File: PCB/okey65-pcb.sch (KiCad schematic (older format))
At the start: 152 parts, among them J1 USB_C_Receptacle_USB2.0, SW1 SW_Push, U1 ATmega32U4-AU, Y1 16MHz

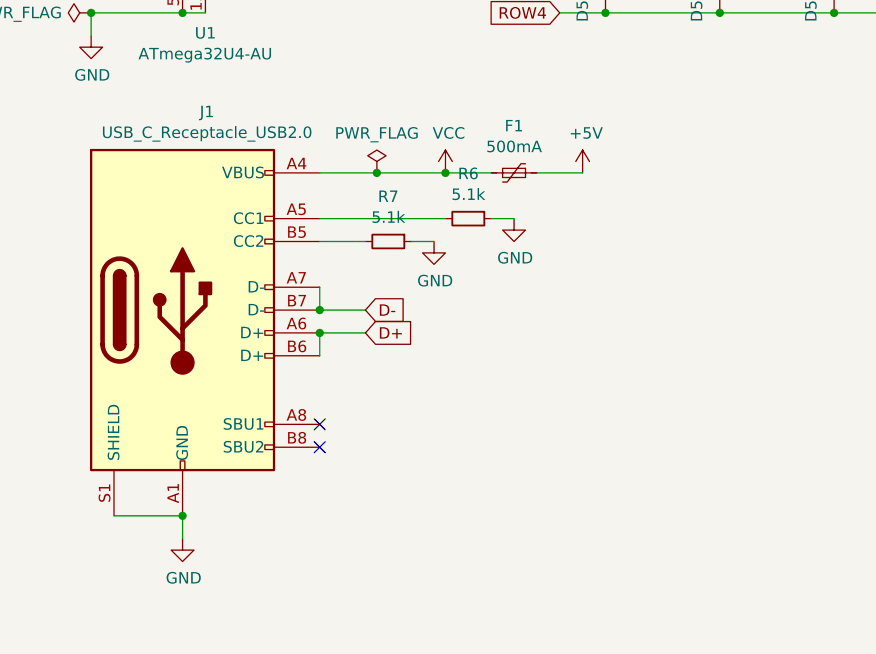
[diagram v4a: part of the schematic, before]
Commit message: General improvements - no ground planes
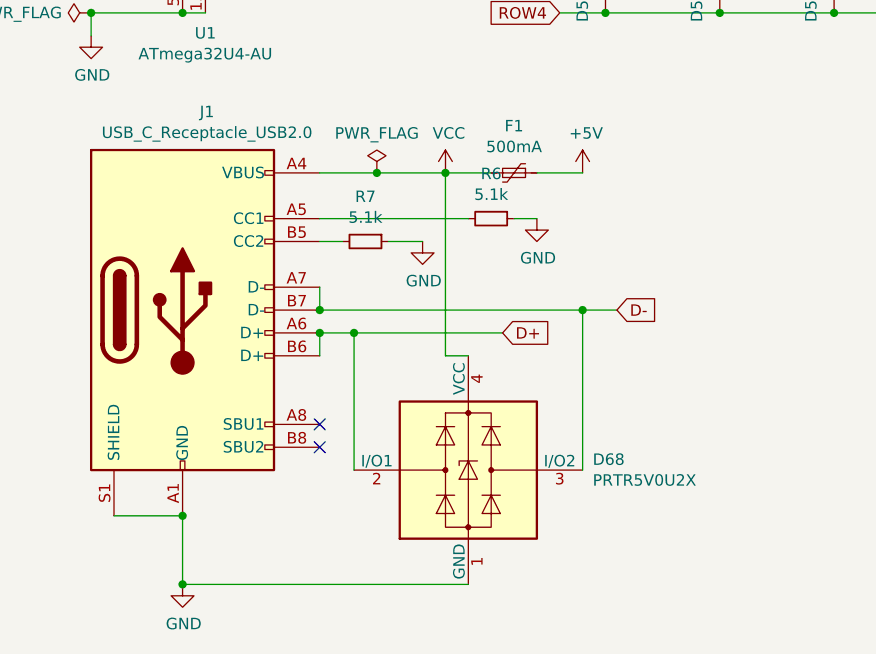
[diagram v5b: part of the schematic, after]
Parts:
- added D68: PRTR5V0U2X, random-keyboard-parts:SOT143B, symbol Power_Protection:PRTR5V0U2X
- C7: footprint Capacitor_SMD:C_0805_2012Metric -> Capacitor_SMD:C_1206_3216Metric
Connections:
- net D+: now also D68.2 (I/O1)
- net D-: now also D68.3 (I/O2)
- net GND: now also D68.1 (GND)
- net VCC: now also D68.4 (VCC)
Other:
- moved on the sheet: R6, R7
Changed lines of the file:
@@
 F 0 "C7" H 1992 4296 50  0000 L CNN
 F 1 "10uF" H 1992 4205 50  0000 L CNN
-F 2 "Capacitor_SMD:C_0805_2012Metric" H 1900 4250 50  0001 C CNN
+F 2 "Capacitor_SMD:C_1206_3216Metric" H 1900 4250 50  0001 C CNN
 F 3 "~" H 1900 4250 50  0001 C CNN
 F 4 "C77075" H 1900 4250 50  0001 C CNN "LCSC"
@@
 Wire Wire Line
 	4200 5700 4400 5700
-Text GLabel 3450 6400 2    50   Input ~ 0
+Text GLabel 4050 6400 2    50   Input ~ 0
 D+
-Text GLabel 3450 6300 2    50   Input ~ 0
+Text GLabel 4550 6300 2    50   Input ~ 0
 D-
 Wire Wire Line
 	3250 6200 3250 6300
 Wire Wire Line
-	3250 6300 3450 6300
+	3250 6300 4400 6300
 Connection ~ 3250 6300
 Wire Wire Line
 	3250 6500 3250 6400
 Wire Wire Line
-	3250 6400 3450 6400
+	3250 6400 3400 6400
 Connection ~ 3250 6400
 $Comp
 L power:GND #PWR017
 U 1 1 61C37D79
-P 2650 7300
-F 0 "#PWR017" H 2650 7050 50  0001 C CNN
-F 1 "GND" H 2655 7127 50  0000 C CNN
-F 2 "" H 2650 7300 50  0001 C CNN
-F 3 "" H 2650 7300 50  0001 C CNN
-	1    2650 7300
+P 2650 7500
+F 0 "#PWR017" H 2650 7250 50  0001 C CNN
+F 1 "GND" H 2655 7327 50  0000 C CNN
+F 2 "" H 2650 7500 50  0001 C CNN
+F 3 "" H 2650 7500 50  0001 C CNN
+	1    2650 7500
 	1    0    0    -1
 $EndComp
 Wire Wire Line
 	2350 7200 2650 7200
-Wire Wire Line
-	2650 7200 2650 7300
-Connection ~ 2650 7200
 $Comp
 L Device:R_Small R7
 U 1 1 61C3A76B
-P 3550 6000
-F 0 "R7" V 3354 6000 50  0000 C CNN
-F 1 "5.1k" V 3445 6000 50  0000 C CNN
-F 2 "Resistor_SMD:R_0805_2012Metric" H 3550 6000 50  0001 C CNN
-F 3 "~" H 3550 6000 50  0001 C CNN
-F 4 "C27834" H 3550 6000 50  0001 C CNN "LCSC"
-	1    3550 6000
+P 3450 6000
+F 0 "R7" V 3254 6000 50  0000 C CNN
+F 1 "5.1k" V 3345 6000 50  0000 C CNN
+F 2 "Resistor_SMD:R_0805_2012Metric" H 3450 6000 50  0001 C CNN
+F 3 "~" H 3450 6000 50  0001 C CNN
+F 4 "C27834" H 3450 6000 50  0001 C CNN "LCSC"
+	1    3450 6000
 	0    1    1    0
 $EndComp
@@
 L Device:R_Small R6
 U 1 1 61C3B0BC
-P 3900 5900
-F 0 "R6" V 3704 5900 50  0000 C CNN
-F 1 "5.1k" V 3795 5900 50  0000 C CNN
-F 2 "Resistor_SMD:R_0805_2012Metric" H 3900 5900 50  0001 C CNN
-F 3 "~" H 3900 5900 50  0001 C CNN
-F 4 "C27834" H 3900 5900 50  0001 C CNN "LCSC"
-	1    3900 5900
+P 4000 5900
+F 0 "R6" V 3804 5900 50  0000 C CNN
+F 1 "5.1k" V 3895 5900 50  0000 C CNN
+F 2 "Resistor_SMD:R_0805_2012Metric" H 4000 5900 50  0001 C CNN
+F 3 "~" H 4000 5900 50  0001 C CNN
+F 4 "C27834" H 4000 5900 50  0001 C CNN "LCSC"
+	1    4000 5900
 	0    1    1    0
 $EndComp
@@
 L power:GND #PWR014
 U 1 1 61C3D0EA
-P 4100 5900
-F 0 "#PWR014" H 4100 5650 50  0001 C CNN
-F 1 "GND" H 4105 5727 50  0000 C CNN
-F 2 "" H 4100 5900 50  0001 C CNN
-F 3 "" H 4100 5900 50  0001 C CNN
-	1    4100 5900
+P 4200 5900
+F 0 "#PWR014" H 4200 5650 50  0001 C CNN
+F 1 "GND" H 4205 5727 50  0000 C CNN
+F 2 "" H 4200 5900 50  0001 C CNN
+F 3 "" H 4200 5900 50  0001 C CNN
+	1    4200 5900
 	1    0    0    -1
 $EndComp
@@
 L power:GND #PWR015
 U 1 1 61C3DC0E
-P 3750 6000
-F 0 "#PWR015" H 3750 5750 50  0001 C CNN
-F 1 "GND" H 3755 5827 50  0000 C CNN
-F 2 "" H 3750 6000 50  0001 C CNN
-F 3 "" H 3750 6000 50  0001 C CNN
-	1    3750 6000
-	1    0    0    -1
-$EndComp
-Wire Wire Line
-	3250 5900 3800 5900
-Wire Wire Line
-	4000 5900 4100 5900
-Wire Wire Line
-	3250 6000 3450 6000
-Wire Wire Line
-	3650 6000 3750 6000
+P 3700 6000
+F 0 "#PWR015" H 3700 5750 50  0001 C CNN
+F 1 "GND" H 3705 5827 50  0000 C CNN
+F 2 "" H 3700 6000 50  0001 C CNN
+F 3 "" H 3700 6000 50  0001 C CNN
+	1    3700 6000
+	1    0    0    -1
+$EndComp
+Wire Wire Line
+	3250 5900 3900 5900
+Wire Wire Line
+	3250 6000 3350 6000
+Wire Wire Line
+	3550 6000 3700 6000
 NoConn ~ 3250 6800
 NoConn ~ 3250 6900
@@
 Connection ~ 2650 1250
 Connection ~ 2650 1400
+$Comp
+L Power_Protection:PRTR5V0U2X D68
+U 1 1 61C886DE
+P 3900 7000
+F 0 "D68" H 4444 7046 50  0000 L CNN
+F 1 "PRTR5V0U2X" H 4444 6955 50  0000 L CNN
+F 2 "random-keyboard-parts:SOT143B" H 3960 7000 50  0001 C CNN
+F 3 "https://assets.nexperia.com/documents/data-sheet/PRTR5V0U2X.pdf" H 3960 7000 50  0001 C CNN
+	1    3900 7000
+	1    0    0    -1
+$EndComp
+Wire Wire Line
+	4400 7000 4400 6300
+Connection ~ 4400 6300
+Wire Wire Line
+	4400 6300 4550 6300
+Wire Wire Line
+	3400 7000 3400 6400
+Connection ~ 3400 6400
+Wire Wire Line
+	3400 6400 4050 6400
+Wire Wire Line
+	3900 7500 2650 7500
+Wire Wire Line
+	2650 7200 2650 7500
+Connection ~ 2650 7200
+Connection ~ 2650 7500
+Wire Wire Line
+	4100 5900 4200 5900
+Wire Wire Line
+	3800 5700 3800 6500
+Wire Wire Line
+	3800 6500 3900 6500
 $EndSCHEMATC

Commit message: v 1.0
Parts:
- added FB1: 60@100MHz, Inductor_SMD:L_1206_3216Metric, symbol Device:Ferrite_Bead_Small
- C1, C2: LCSC C1804 -> (none)
- C3: LCSC C116352 -> (none)
- C4, C5, C6: LCSC C286511 -> (none)
- C7: LCSC C77075 -> (none)
- D1, D10, D11, D12, D13, D14, D15, D16, D17, D18, D19, D2, D20, D21, D22, D23, D24, D25, D26, D27, D28, D29, D3, D30, D31, D32, D33, D34, D35, D36, D37, D38, D39, D4, D40, D41, D42, D43, D44, D45, D46, D47, D48, D49, D5, D50, D51, D52, D53, D54, D55, D56, D57, D58, D59, D6, D60, D61, D62, D63, D64, D65, D7, D8, D9: LCSC C81598 -> (none)
- D66, D67: LCSC C401114 -> (none)
- F1: LCSC C883125 -> (none)
- J1: LCSC C136423 -> (none)
- R1, R4: LCSC C406725 -> (none)
- R2, R3: LCSC C25295 -> (none)
- R5, R8: value 68 -> 150; LCSC C17802 -> (none)
- R6, R7: LCSC C27834 -> (none)
- SW1: LCSC C221929 -> (none)
- U1: LCSC C44854 -> (none)
- Y1: LCSC C213410 -> (none)
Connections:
- net GND: now also FB1.1; no longer J1.S1 (SHIELD)
- new net: FB1.2, J1.S1 (SHIELD)
